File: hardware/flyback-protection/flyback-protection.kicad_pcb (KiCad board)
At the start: 2 copper layers, 30 x 20 mm, 3 parts, among them J1 Screw_Terminal_01x02, J3 Screw_Terminal_01x02

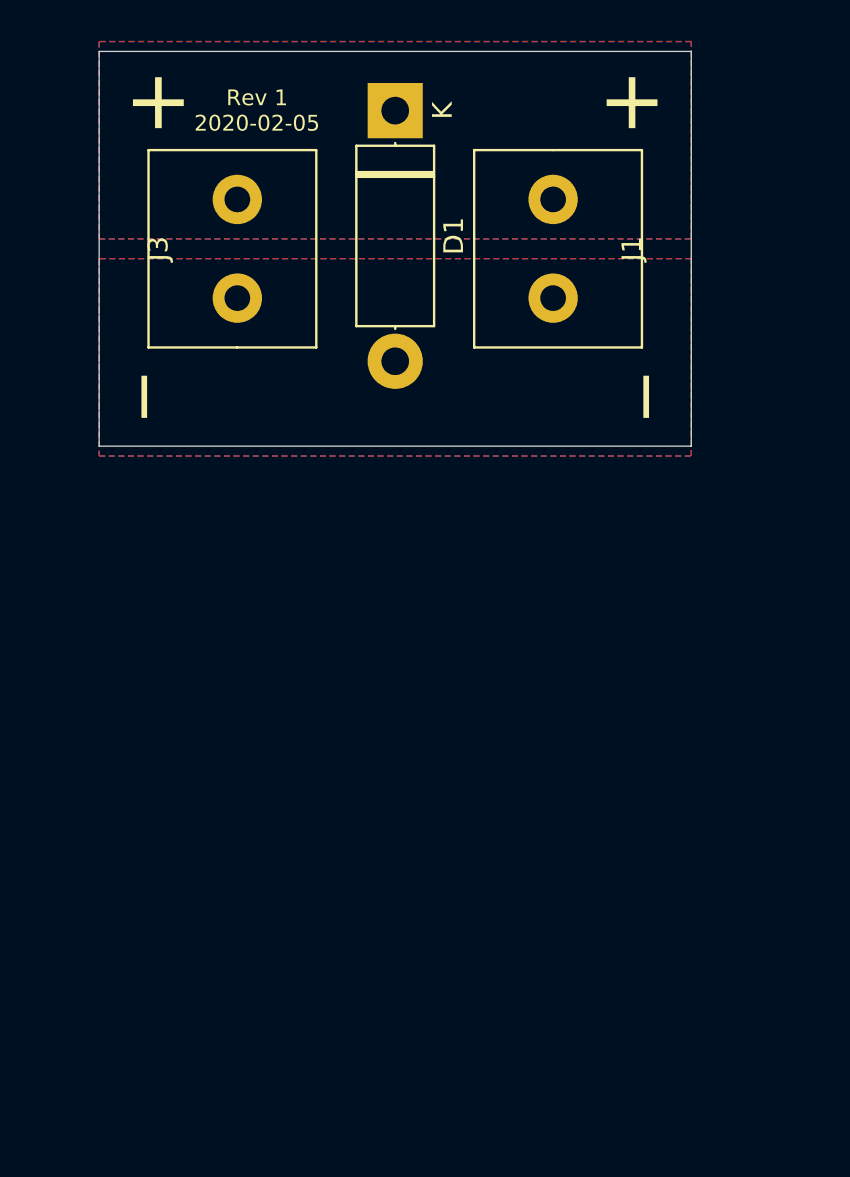
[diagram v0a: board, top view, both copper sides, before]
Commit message: Changed to M5 connector for flyback
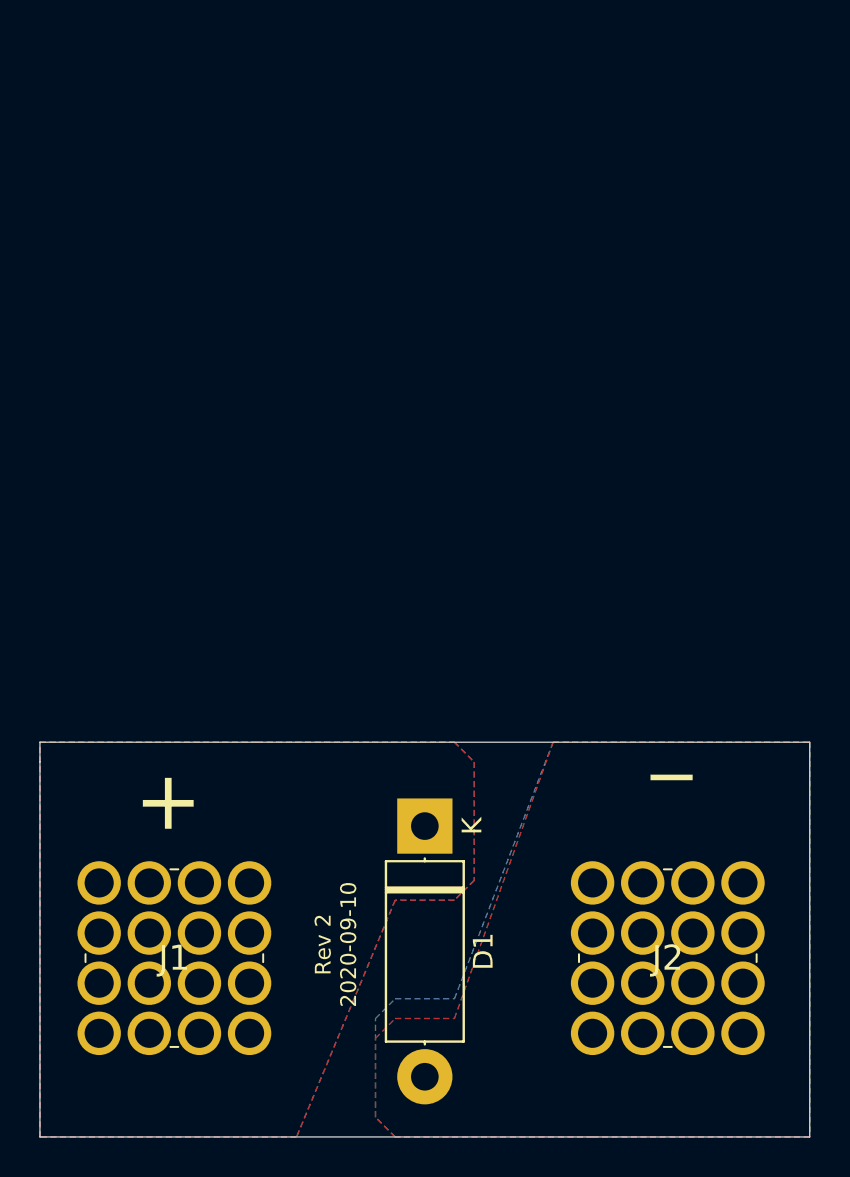
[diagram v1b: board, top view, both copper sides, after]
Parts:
- removed J3: Screw_Terminal_01x02, Highside-powerdistribution:Phoenix_TB_2-1935776
- added J2: M5, private:M5_7461383, F.Cu at (125.0, 99.8)
- J1: value Screw_Terminal_01x02 -> M5; footprint Highside-powerdistribution:Phoenix_TB_2-1935776 -> private:M5_7461383
- moved J1 45.9 mm to (100.0, 99.8), turned to 0 degrees
- moved D1 36.3 mm to (116.5, 89.2)
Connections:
- J1 pad 1: GND -> +12V
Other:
- board size 30 x 20 mm -> 39 x 20 mm
- board text added: "Rev 2 2020-09-10"
- board text removed: "Rev 1 2020-02-05"
